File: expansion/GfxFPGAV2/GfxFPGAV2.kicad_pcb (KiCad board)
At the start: 4 copper layers, 100 x 100 mm, 72 parts, among them J1 JTAG, J101 D68K_64PIN_BOARD, J501 VGA Out, U101 SN74LS125ADR, U102 LD1117S12TR_SOT223, U2 XC6SLX9-FTG256, U201 SN74LVC8T245PWR, U202 SN74LVC8T245PWR, U203 SN74LVC8T245PWR, U204 SN74LVC8T245PWR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

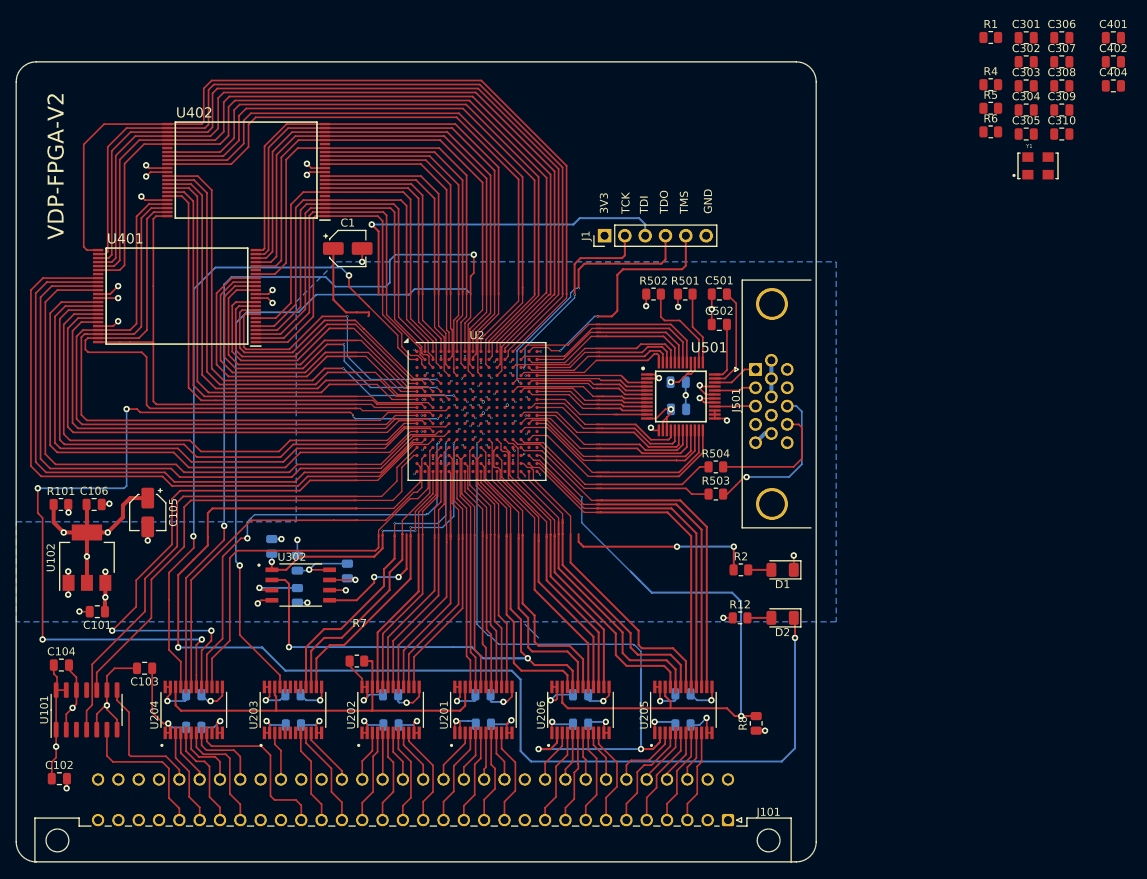
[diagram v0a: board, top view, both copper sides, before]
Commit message: Working on VGA baord layout
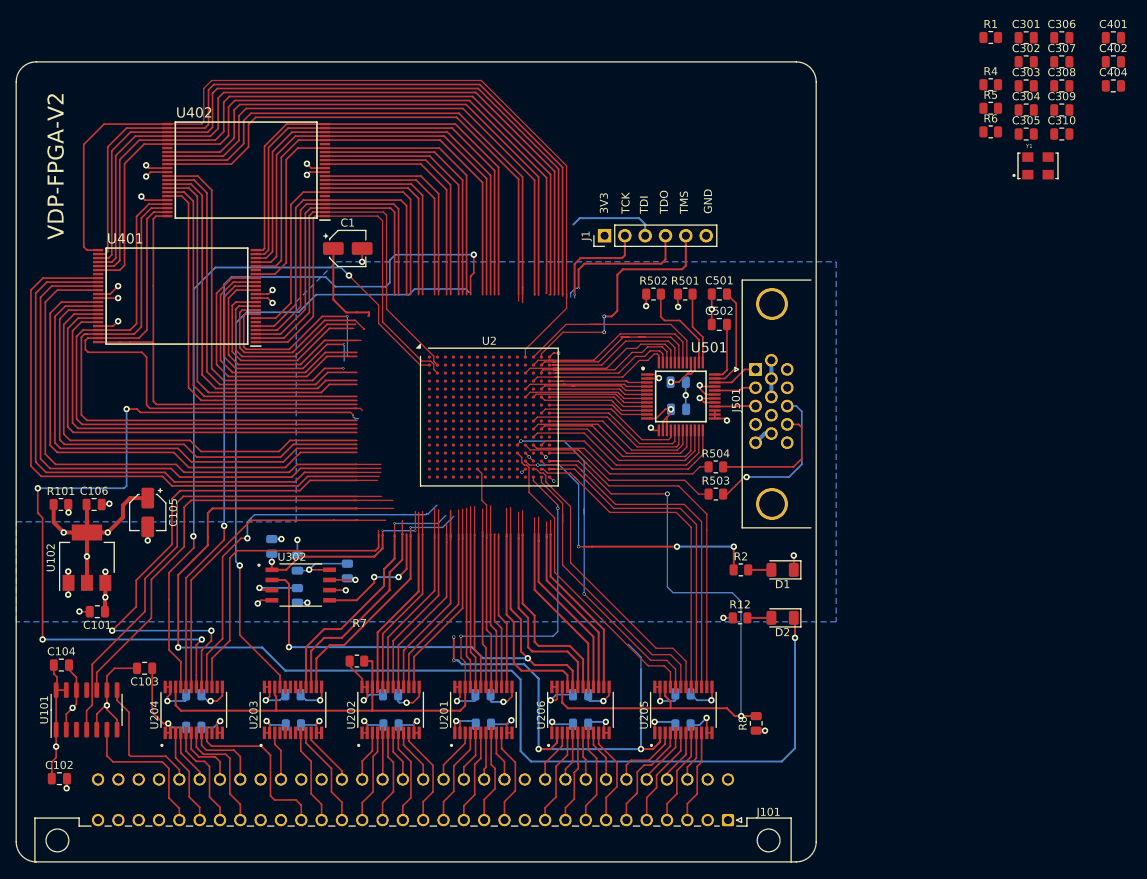
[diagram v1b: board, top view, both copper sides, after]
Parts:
- moved U2 1.70 mm to (159.2, 94.4)
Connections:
- U2 pad B15: /FPGA/R3 -> /FPGA/R2
- U2 pad B16: /FPGA/R2 -> /FPGA/R3
- U2 pad C15: /FPGA/R6 -> /FPGA/R5
- U2 pad C16: /FPGA/R5 -> /FPGA/R6
- U2 pad N14: /FPGA/D0 -> unconnected-(U2A-IO_L45P_A1_M1LDQS_1-PadN14)
- U2 pad N16: unconnected-(U2A-IO_L45N_A0_M1LDQSN_1-PadN16) -> /FPGA/D0
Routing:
- net /FPGA/~{BUSEN}: track 54.9 -> 91.1 mm, vias 0 -> 2
- net /FPGA/TDI: track 45.4 -> 11.1 mm, vias 1 -> 0
- net /FPGA/DATA_DIR: track 79.1 -> 58.7 mm, vias 3 -> 4
- net /FPGA/SRAM_D28: track 62.1 -> 46.3 mm, vias 2 -> 1
- net /FPGA/FPGA_DONE: track 23.5 -> 39.1 mm, vias 2 -> 4
- net /FPGA/TDO: track 32.2 -> 18.4 mm, vias 2 -> 1
- net /FPGA/SRAM_D5: track 44.6 -> 30.9 mm, vias 2 -> 1
- net /FPGA/D8: track 36.8 -> 23.7 mm
- net /FPGA/SRAM_D0: track 38.4 -> 25.3 mm, vias 2 -> 1
- net /FPGA/SRAM_A11: track 108.2 -> 95.2 mm
- net /FPGA/SRAM_D29: track 60.9 -> 48.0 mm
- net /FPGA/SRAM_D14: track 71.8 -> 59.1 mm
- net /FPGA/TCK: track 25.3 -> 13.4 mm, vias 2 -> 1
- net /FPGA/SRAM_A10: track 105.9 -> 94.1 mm
- net /FPGA/SRAM_D2: track 36.5 -> 24.7 mm
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
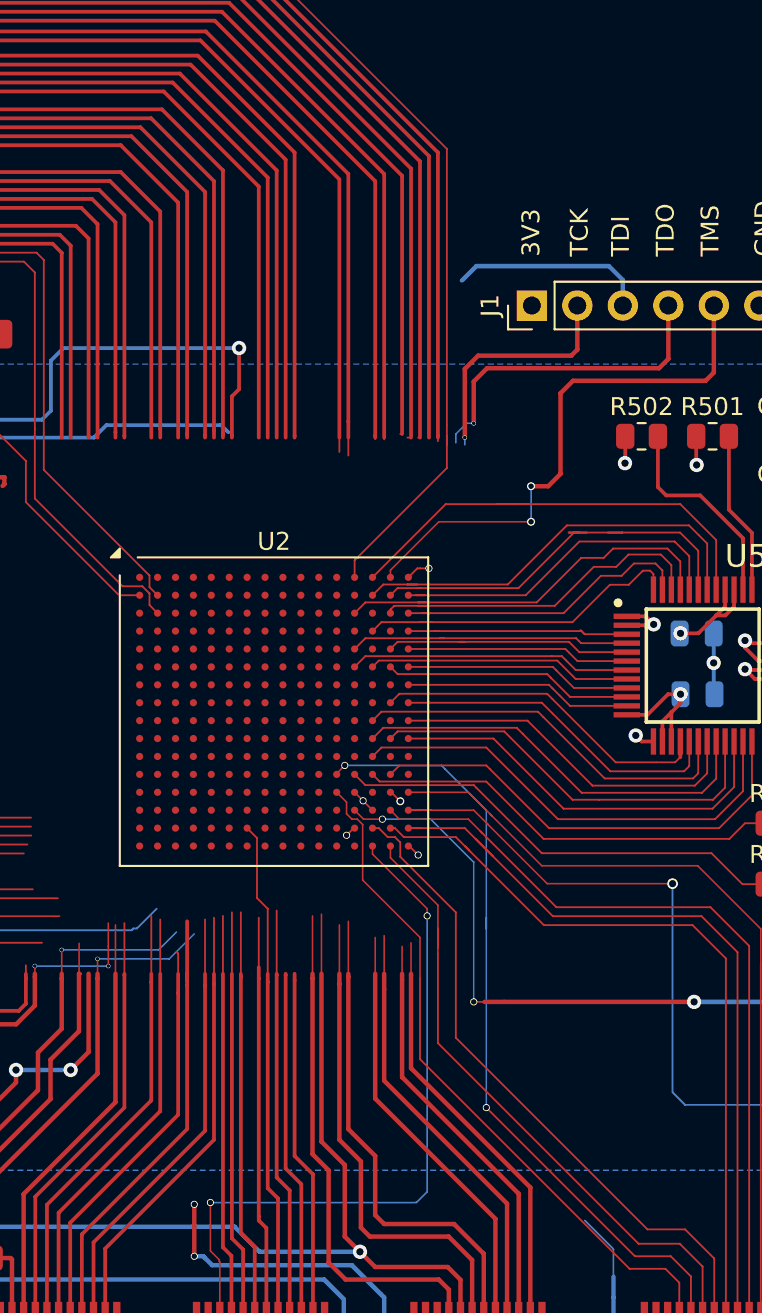
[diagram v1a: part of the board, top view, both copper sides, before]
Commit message: More routing on the VGA board
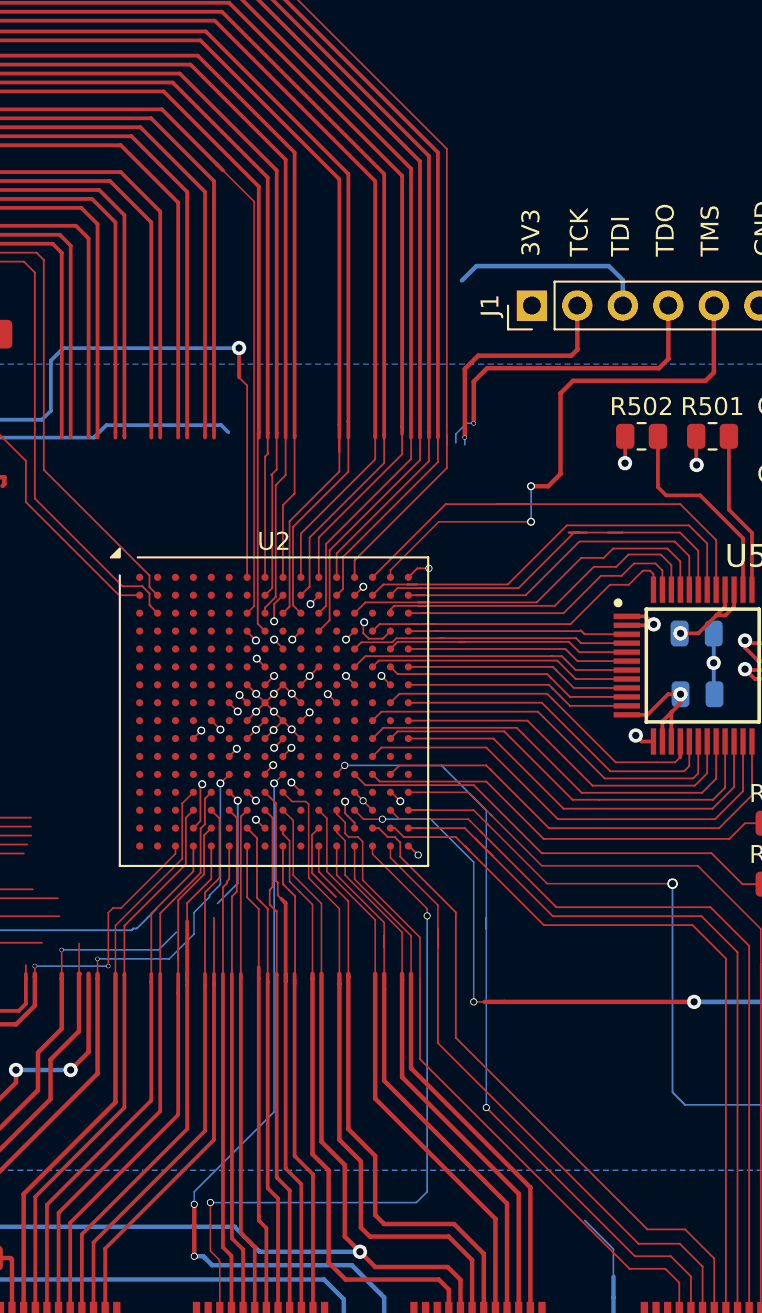
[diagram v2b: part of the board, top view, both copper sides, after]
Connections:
- R1 pad 1: /FPGA/D10 -> /FPGA/FPGA_M1
- R4 pad 2: /FPGA/D11 -> /FPGA/D12
- U2 pad A8: /FPGA/SRAM_A17 -> /FPGA/SRAM_A18
- U2 pad A9: /FPGA/SRAM_D27 -> /FPGA/SRAM_A15
- U2 pad B8: /FPGA/SRAM_A16 -> /FPGA/SRAM_A17
- U2 pad C8: /FPGA/SRAM_A18 -> /FPGA/SRAM_A16
- U2 pad C9: unconnected-(U2A-IO_L34P_GCLK19_0-PadC9) -> /FPGA/SRAM_D27
- U2 pad D9: /FPGA/SRAM_A15 -> unconnected-(U2A-IO_L40N_0-PadD9)
- U2 pad M10: /FPGA/D12 -> unconnected-(U2B-IO_L16N_VREF_2-PadM10)
- U2 pad M11: /FPGA/D8 -> unconnected-(U2B-IO_L2N_CMPMOSI_2-PadM11)
- U2 pad N11: /FPGA/D10 -> /FPGA/FPGA_M1
- U2 pad N12: /FPGA/D7 -> unconnected-(U2B-IO_L12P_D1_MISO2_2-PadN12)
- U2 pad N8: /FPGA/A3 -> /FPGA/A2
- U2 pad P11: /FPGA/D9 -> /FPGA/D11
- U2 pad P12: unconnected-(U2B-IO_L12N_D2_MISO3_2-PadP12) -> /FPGA/D7
- U2 pad P8: /FPGA/A2 -> /FPGA/A3
- U2 pad P9: /FPGA/A1 -> /FPGA/D14
- U2 pad R12: unconnected-(U2A-IO_L52P_M1DQ14_1-PadR12) -> /FPGA/D9
- U2 pad R9: /FPGA/D14 -> /FPGA/D15
- U2 pad T11: /FPGA/D11 -> /FPGA/D12
- U2 pad T12: unconnected-(U2A-IO_L52N_M1DQ15_1-PadT12) -> /FPGA/D10
- U2 pad T13: unconnected-(U2A-IO_L51N_M1DQ13_1-PadT13) -> /FPGA/D8
- U2 pad T9: /FPGA/D15 -> /FPGA/A1
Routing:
- net /FPGA/DATA_DIR: track 58.7 -> 84.8 mm, vias 4 -> 5
- net +3V3: track 81.5 -> 99.6 mm, vias 24 -> 41
- net /FPGA/SRAM_A11: track 95.2 -> 108.4 mm
- net /FPGA/SRAM_D27: track 66.4 -> 78.2 mm
- net /FPGA/SRAM_A10: track 94.1 -> 105.9 mm
- net /FPGA/SRAM_A19: track 58.7 -> 70.0 mm
- net /FPGA/~{SRAM_WE}: track 56.8 -> 67.9 mm
- net /FPGA/SRAM_A13: track 97.6 -> 108.7 mm
- net /FPGA/A2: track 19.5 -> 30.5 mm
- net /FPGA/SRAM_D24: track 69.5 -> 80.4 mm
- net /FPGA/SRAM_A16: track 61.6 -> 72.0 mm
- net /FPGA/SRAM_D26: track 68.4 -> 78.7 mm
- net /FPGA/SRAM_A12: track 96.3 -> 106.6 mm
- net /FPGA/SRAM_A9: track 92.9 -> 103.1 mm
- net +1V2: track 27.0 -> 36.9 mm, vias 3 -> 10
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
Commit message: VGA board v2 routing done
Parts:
- removed C310: 100nF, Capacitor_SMD:C_0805_2012Metric
- added G***: LOGO, Ddraig:Ddraig68k-26mm, F.Cu at (184.4, 57.2)
- C301, C302, C303, C304, C305, C306, C307, C308, C309, C401, C402, C404, R1, R4, R5, R6, Y1: moved to B.Cu
- moved C309 124.9 mm to (116.4, 106.3), turned to -90 degrees
- moved C402 93.4 mm to (154.6, 93.6), turned to 180 degrees
- moved C306 88.4 mm to (157.5, 96.5), turned to 90 degrees
- moved R4 85.8 mm to (175.5, 125.1), turned to 180 degrees
- moved C404 85.7 mm to (165.0, 99.2), turned to 180 degrees
- moved C401 85.2 mm to (163.5, 89.8), turned to 180 degrees
- moved C307 85.1 mm to (156.1, 90.8), turned to 180 degrees
- moved C301 82.7 mm to (154.1, 87.5), turned to -90 degrees
- moved R6 81.7 mm to (142.9, 79.8), turned to 180 degrees
- moved R1 81.2 mm to (161.1, 100.9), turned to 180 degrees
- moved C308 81.0 mm to (162.2, 96.2)
- moved Y1 80.4 mm to (159.9, 106.2), turned to 180 degrees
- moved R5 80.4 mm to (154.2, 99.2), turned to 180 degrees
- moved C302 77.7 mm to (168.0, 101.4), turned to -90 degrees
- moved C303 76.6 mm to (158.3, 88.4), turned to 180 degrees
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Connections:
- U2 pad A2: /FPGA/SRAM_A1 -> /FPGA/SRAM_A2
- U2 pad B6: unconnected-(U2A-IO_L4P_0-PadB6) -> /FPGA/SRAM_D22
- U2 pad C1: unconnected-(U2B-IO_L50P_M3WE_3-PadC1) -> /FPGA/SRAM_D0
- U2 pad C3: /FPGA/SRAM_A2 -> /FPGA/SRAM_A1
- U2 pad D1: unconnected-(U2B-IO_L49N_M3A2_3-PadD1) -> /FPGA/SRAM_D2
- U2 pad D6: /FPGA/SRAM_D22 -> unconnected-(U2A-IO_L7P_0-PadD6)
- U2 pad E1: /FPGA/SRAM_D3 -> /FPGA/SRAM_D5
- U2 pad E2: /FPGA/SRAM_D2 -> /FPGA/SRAM_D3
- U2 pad E4: /FPGA/SRAM_D0 -> unconnected-(U2B-IO_L54P_M3RESET_3-PadE4)
- U2 pad F4: /FPGA/SRAM_D5 -> unconnected-(U2B-IO_L53P_M3CKE_3-PadF4)
- U2 pad L1: /FPGA/SRAM_D12 -> /FPGA/SRAM_D13
- U2 pad L3: /FPGA/SRAM_D13 -> /FPGA/SRAM_D12
- U2 pad L4: /FPGA/SRAM_D11 -> /FPGA/SRAM_D10
- U2 pad L5: /FPGA/SRAM_D10 -> /FPGA/SRAM_D11
- U2 pad M1: /FPGA/SRAM_D9 -> /FPGA/~{LDS}
- U2 pad M11: unconnected-(U2B-IO_L2N_CMPMOSI_2-PadM11) -> /FPGA/D13
- U2 pad M2: /FPGA/SRAM_D8 -> /FPGA/SRAM_D9
- U2 pad M3: /FPGA/~{LDS} -> /FPGA/SRAM_D8
- U2 pad M5: /FPGA/A19 -> unconnected-(U2B-IO_L2P_3-PadM5)
- U2 pad M7: /FPGA/HOST_CLK -> /FPGA/A19
- U2 pad N12: unconnected-(U2B-IO_L12P_D1_MISO2_2-PadN12) -> /FPGA/HOST_CLK
- U2 pad N9: /FPGA/D13 -> unconnected-(U2B-IO_L14P_D11_2-PadN9)
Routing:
- net /FPGA/FLASH_CLK: track 6.60 -> 61.1 mm, vias 1 -> 2
- net /FPGA/FLASH_DO: track 0.00 -> 51.4 mm, vias 0 -> 2
- net /FPGA/D14: track 75.4 -> 32.3 mm, vias 2 -> 0
- net GND: track 160.6 -> 196.4 mm, vias 51 -> 64
- net /FPGA/~{AS}: track 38.6 -> 74.3 mm, vias 0 -> 2
- net /FPGA/FPGA_PROGB: track 12.0 -> 47.1 mm, vias 0 -> 2
- net /FPGA/DATA_DIR: track 84.8 -> 59.3 mm, vias 5 -> 4
- net /FPGA/TDI: track 11.1 -> 35.4 mm, vias 0 -> 1
- net /FPGA/FLASH_DI: track 16.0 -> 40.3 mm
- net +3V3: track 99.6 -> 120.3 mm, vias 41 -> 51
- net /FPGA/TDO: track 18.4 -> 38.4 mm, vias 1 -> 2
- net /FPGA/HOST_CLK: track 78.8 -> 59.1 mm, vias 1 -> 4
- net /FPGA/SRAM_D28: track 46.3 -> 64.5 mm, vias 1 -> 2
- net /FPGA/TCK: track 13.4 -> 29.7 mm
- net /FPGA/SRAM_D29: track 48.0 -> 62.6 mm
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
